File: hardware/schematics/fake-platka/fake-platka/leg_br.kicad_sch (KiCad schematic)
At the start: 20 parts, among them J3 B2B-EH-A, J4 B2B-EH-A, J5 B2B-EH-A, J6 B2B-EH-A, J7 B2B-EH-A, J8 XT60PW-F, J9 XT60PW-F, U2 TB67H450AFNG_EL, U3 TB67H450AFNG_EL

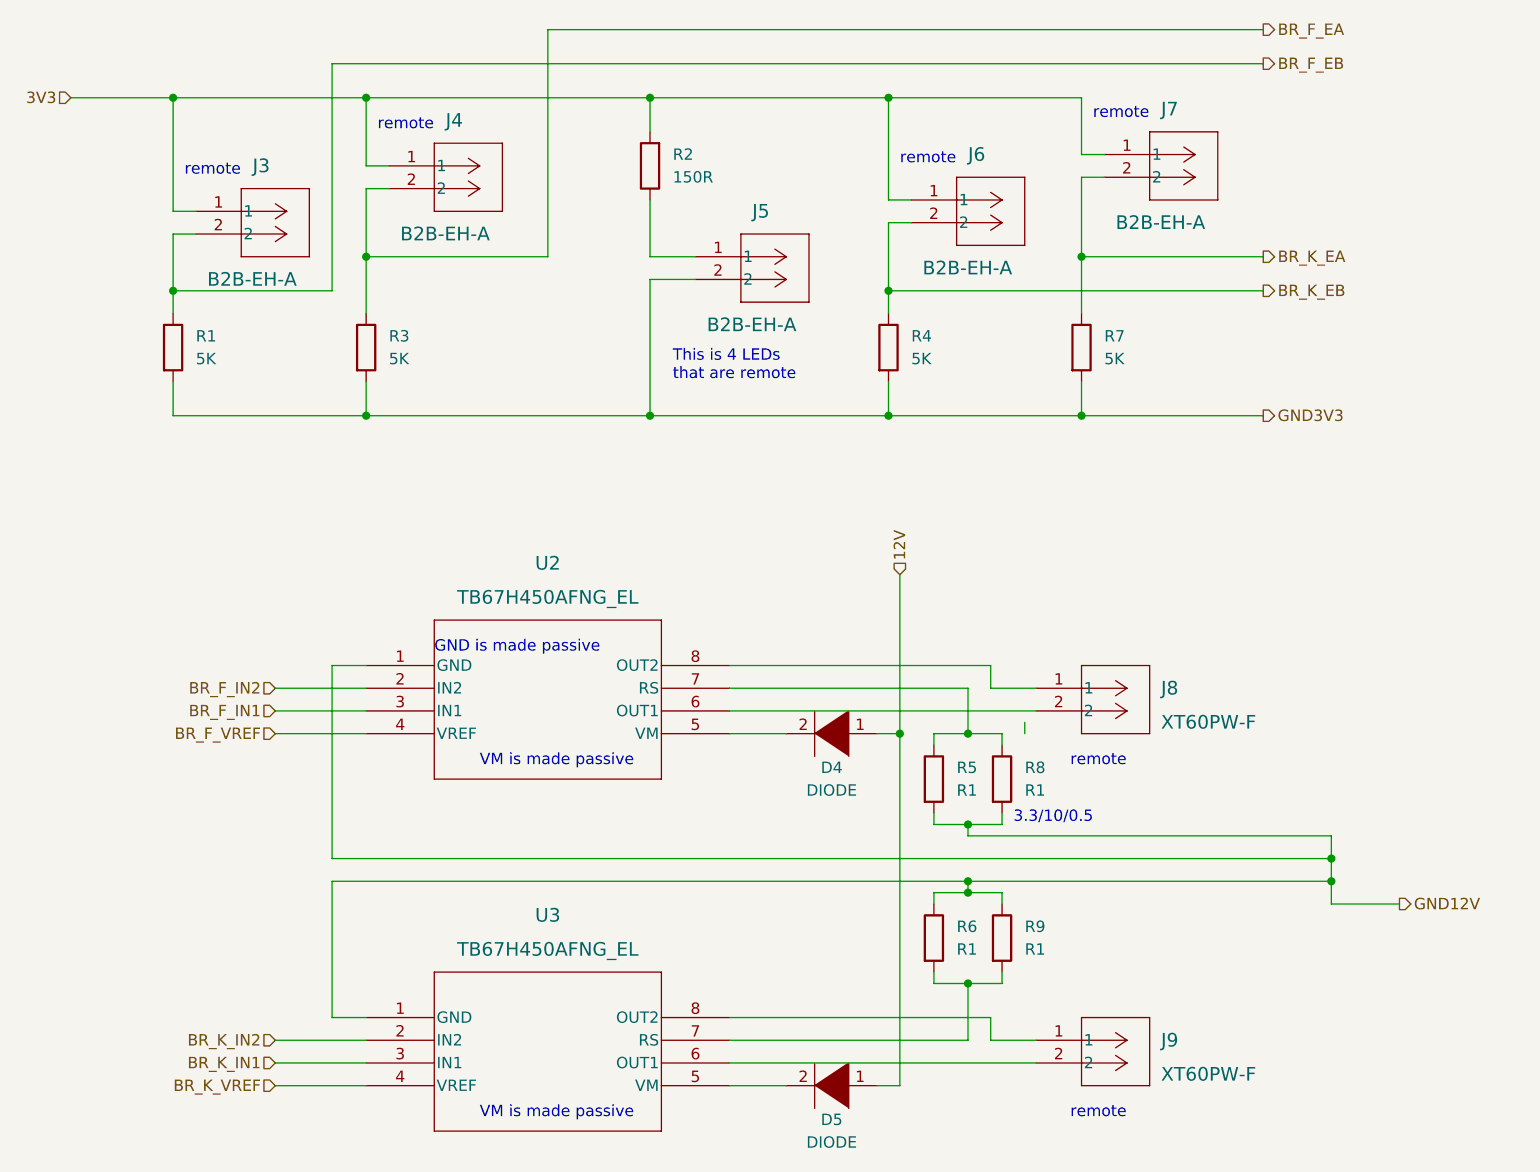
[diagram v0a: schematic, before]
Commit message: added all components to the schematic and pcb
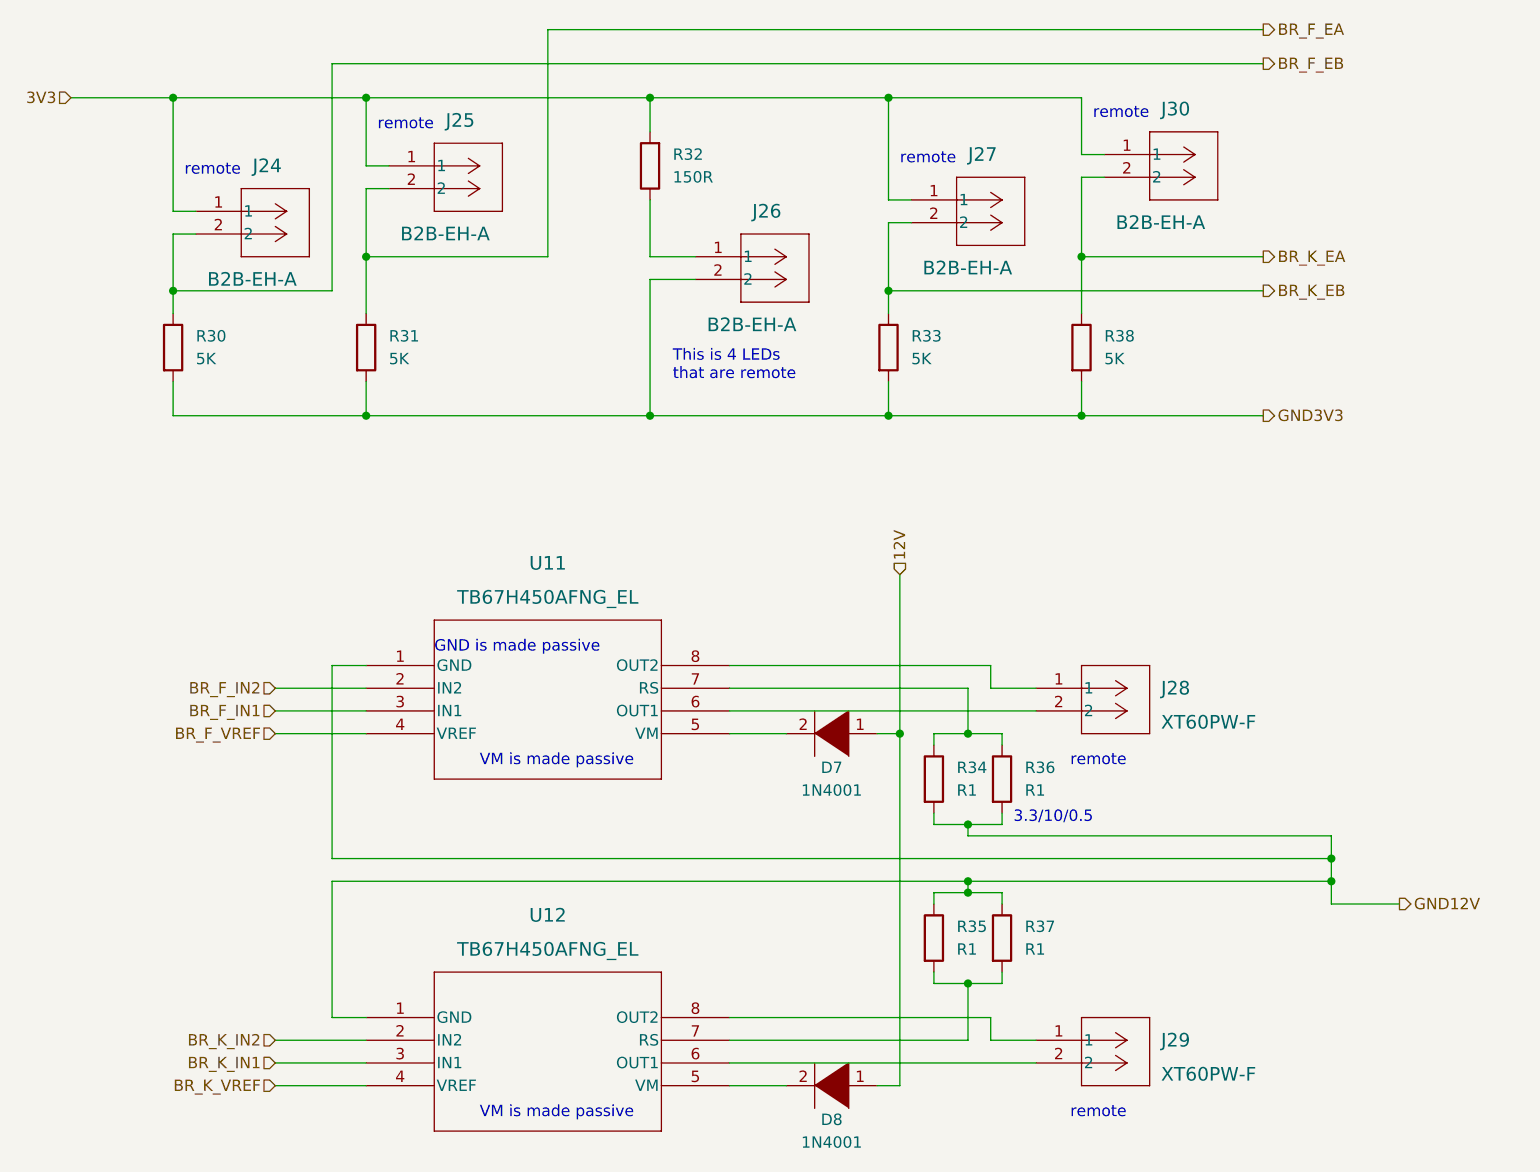
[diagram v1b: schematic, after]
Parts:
- D7: renamed from D4; value DIODE -> 1N4001
- D8: renamed from D5; value DIODE -> 1N4001
- renumbered J3 to J24, J4 to J25, J5 to J26, J6 to J27, J8 to J28, J9 to J29, J7 to J30, R1 to R30, R3 to R31, R2 to R32, R4 to R33, R5 to R34, R6 to R35, R8 to R36, R9 to R37, R7 to R38, U2 to U11, U3 to U12
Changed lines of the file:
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@@
-    (stroke (width 0) (type default) (color 0 0 0 0))
-  )
-  (wire (pts (xy 143.51 111.76) (xy 143.51 110.49))
     (stroke (width 0) (type default) (color 0 0 0 0))
   )
@@
   (symbol (lib_id "Device:R") (at 149.86 68.58 0) (unit 1)
     (in_bom yes) (on_board yes) (fields_autoplaced)
-    (property "Reference" "R7" (id 0) (at 152.4 67.3099 0)
+    (property "Reference" "R38" (id 0) (at 152.4 67.3099 0)
       (effects (font (size 1.27 1.27)) (justify left))
     )
@@
   (symbol (lib_id "Device:R") (at 69.85 68.58 0) (unit 1)
     (in_bom yes) (on_board yes) (fields_autoplaced)
-    (property "Reference" "R3" (id 0) (at 72.39 67.3099 0)
+    (property "Reference" "R31" (id 0) (at 72.39 67.3099 0)
       (effects (font (size 1.27 1.27)) (justify left))
     )
@@
   (symbol (lib_id "library:B2B-EH-A_LFSN") (at 106.68 58.42 0) (unit 1)
     (in_bom yes) (on_board yes)
-    (property "Reference" "J5" (id 0) (at 113.03 53.34 0)
+    (property "Reference" "J26" (id 0) (at 113.03 53.34 0)
       (effects (font (size 1.524 1.524)) (justify left))
     )
@@
   (symbol (lib_id "library:B2B-EH-A_LFSN") (at 72.39 48.26 0) (unit 1)
     (in_bom yes) (on_board yes)
-    (property "Reference" "J4" (id 0) (at 78.74 43.18 0)
+    (property "Reference" "J25" (id 0) (at 78.74 43.18 0)
       (effects (font (size 1.524 1.524)) (justify left))
     )
@@
   (symbol (lib_id "library:XT60PW-F") (at 144.78 146.05 0) (unit 1)
     (in_bom yes) (on_board yes) (fields_autoplaced)
-    (property "Reference" "J9" (id 0) (at 158.75 146.05 0)
+    (property "Reference" "J29" (id 0) (at 158.75 146.05 0)
       (effects (font (size 1.524 1.524)) (justify left))
     )
@@
   (symbol (lib_id "library:B2B-EH-A_LFSN") (at 50.8 53.34 0) (unit 1)
     (in_bom yes) (on_board yes)
-    (property "Reference" "J3" (id 0) (at 57.15 48.26 0)
+    (property "Reference" "J24" (id 0) (at 57.15 48.26 0)
       (effects (font (size 1.524 1.524)) (justify left))
     )
@@
   (symbol (lib_id "Device:R") (at 140.97 134.62 0) (unit 1)
     (in_bom yes) (on_board yes) (fields_autoplaced)
-    (property "Reference" "R9" (id 0) (at 143.51 133.3499 0)
+    (property "Reference" "R37" (id 0) (at 143.51 133.3499 0)
       (effects (font (size 1.27 1.27)) (justify left))
     )
@@
   (symbol (lib_id "pspice:DIODE") (at 121.92 151.13 180) (unit 1)
     (in_bom yes) (on_board yes)
-    (property "Reference" "D5" (id 0) (at 121.92 154.94 0))
-    (property "Value" "DIODE" (id 1) (at 121.92 157.48 0))
+    (property "Reference" "D8" (id 0) (at 121.92 154.94 0))
+    (property "Value" "1N4001" (id 1) (at 121.92 157.48 0))
     (property "Footprint" "Diode_THT:D_DO-41_SOD81_P7.62mm_Horizontal" (id 2) (at 121.92 151.13 0)
       (effects (font (size 1.27 1.27)) hide)
@@
   (symbol (lib_id "library:B2B-EH-A_LFSN") (at 152.4 46.99 0) (unit 1)
     (in_bom yes) (on_board yes)
-    (property "Reference" "J7" (id 0) (at 158.75 41.91 0)
+    (property "Reference" "J30" (id 0) (at 158.75 41.91 0)
       (effects (font (size 1.524 1.524)) (justify left))
     )
@@
   (symbol (lib_id "library:B2B-EH-A_LFSN") (at 130.81 52.07 0) (unit 1)
     (in_bom yes) (on_board yes)
-    (property "Reference" "J6" (id 0) (at 137.16 46.99 0)
+    (property "Reference" "J27" (id 0) (at 137.16 46.99 0)
       (effects (font (size 1.524 1.524)) (justify left))
     )
@@
   (symbol (lib_name "TB67H450AFNG_EL_1") (lib_id "library:TB67H450AFNG_EL") (at 69.85 104.14 0) (unit 1)
     (in_bom yes) (on_board yes) (fields_autoplaced)
-    (property "Reference" "U2" (id 0) (at 90.17 92.71 0)
+    (property "Reference" "U11" (id 0) (at 90.17 92.71 0)
       (effects (font (size 1.524 1.524)))
     )
@@
   (symbol (lib_id "Device:R") (at 133.35 116.84 0) (unit 1)
     (in_bom yes) (on_board yes) (fields_autoplaced)
-    (property "Reference" "R5" (id 0) (at 135.89 115.5699 0)
+    (property "Reference" "R34" (id 0) (at 135.89 115.5699 0)
       (effects (font (size 1.27 1.27)) (justify left))
     )
@@
   (symbol (lib_id "Device:R") (at 128.27 68.58 0) (unit 1)
     (in_bom yes) (on_board yes) (fields_autoplaced)
-    (property "Reference" "R4" (id 0) (at 130.81 67.3099 0)
+    (property "Reference" "R33" (id 0) (at 130.81 67.3099 0)
       (effects (font (size 1.27 1.27)) (justify left))
     )
@@
   (symbol (lib_id "library:TB67H450AFNG_EL") (at 69.85 143.51 0) (unit 1)
     (in_bom yes) (on_board yes)
-    (property "Reference" "U3" (id 0) (at 90.17 132.08 0)
+    (property "Reference" "U12" (id 0) (at 90.17 132.08 0)
       (effects (font (size 1.524 1.524)))
     )
@@
   (symbol (lib_id "Device:R") (at 101.6 48.26 180) (unit 1)
     (in_bom yes) (on_board yes) (fields_autoplaced)
-    (property "Reference" "R2" (id 0) (at 104.14 46.9899 0)
+    (property "Reference" "R32" (id 0) (at 104.14 46.9899 0)
       (effects (font (size 1.27 1.27)) (justify right))
     )
@@
   (symbol (lib_id "pspice:DIODE") (at 121.92 111.76 180) (unit 1)
     (in_bom yes) (on_board yes)
-    (property "Reference" "D4" (id 0) (at 121.92 115.57 0))
-    (property "Value" "DIODE" (id 1) (at 121.92 118.11 0))
+    (property "Reference" "D7" (id 0) (at 121.92 115.57 0))
+    (property "Value" "1N4001" (id 1) (at 121.92 118.11 0))
     (property "Footprint" "Diode_THT:D_DO-41_SOD81_P7.62mm_Horizontal" (id 2) (at 121.92 111.76 0)
       (effects (font (size 1.27 1.27)) hide)
@@
   (symbol (lib_id "library:XT60PW-F") (at 144.78 106.68 0) (unit 1)
     (in_bom yes) (on_board yes) (fields_autoplaced)
-    (property "Reference" "J8" (id 0) (at 158.75 106.68 0)
+    (property "Reference" "J28" (id 0) (at 158.75 106.68 0)
       (effects (font (size 1.524 1.524)) (justify left))
     )
@@
   (symbol (lib_id "Device:R") (at 48.26 68.58 0) (unit 1)
     (in_bom yes) (on_board yes) (fields_autoplaced)
-    (property "Reference" "R1" (id 0) (at 50.8 67.3099 0)
+    (property "Reference" "R30" (id 0) (at 50.8 67.3099 0)
       (effects (font (size 1.27 1.27)) (justify left))
     )
@@
   (symbol (lib_id "Device:R") (at 133.35 134.62 0) (unit 1)
     (in_bom yes) (on_board yes) (fields_autoplaced)
-    (property "Reference" "R6" (id 0) (at 135.89 133.3499 0)
+    (property "Reference" "R35" (id 0) (at 135.89 133.3499 0)
       (effects (font (size 1.27 1.27)) (justify left))
     )
@@
   (symbol (lib_id "Device:R") (at 140.97 116.84 0) (unit 1)
     (in_bom yes) (on_board yes) (fields_autoplaced)
-    (property "Reference" "R8" (id 0) (at 143.51 115.5699 0)
-      (effects (font (size 1.27 1.27)) (justify left))
-    )
+    (property "Reference" "R36" (id 0) (at 143.51 115.5699 0)
+      (effects (font (size 1.27 1.27)) (justify left))
+    )

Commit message: working on pcb and documentation
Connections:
- net 12V: now also R32.2
- net 3V3: no longer R32.2
- net GND12V: now also J26.2
- net GND3V3: no longer J26.2
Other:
- company: (none) -> By Andrey Shefa
- title: (none) -> First pcb for quadruped robot v3
- moved on the sheet: J24, J25, R30, R31
